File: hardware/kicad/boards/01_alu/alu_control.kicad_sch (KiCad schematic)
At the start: 8 parts, among them U155 KM28C64A, U156 KM28C64A, U171 74AHC541, U172 74AHC541

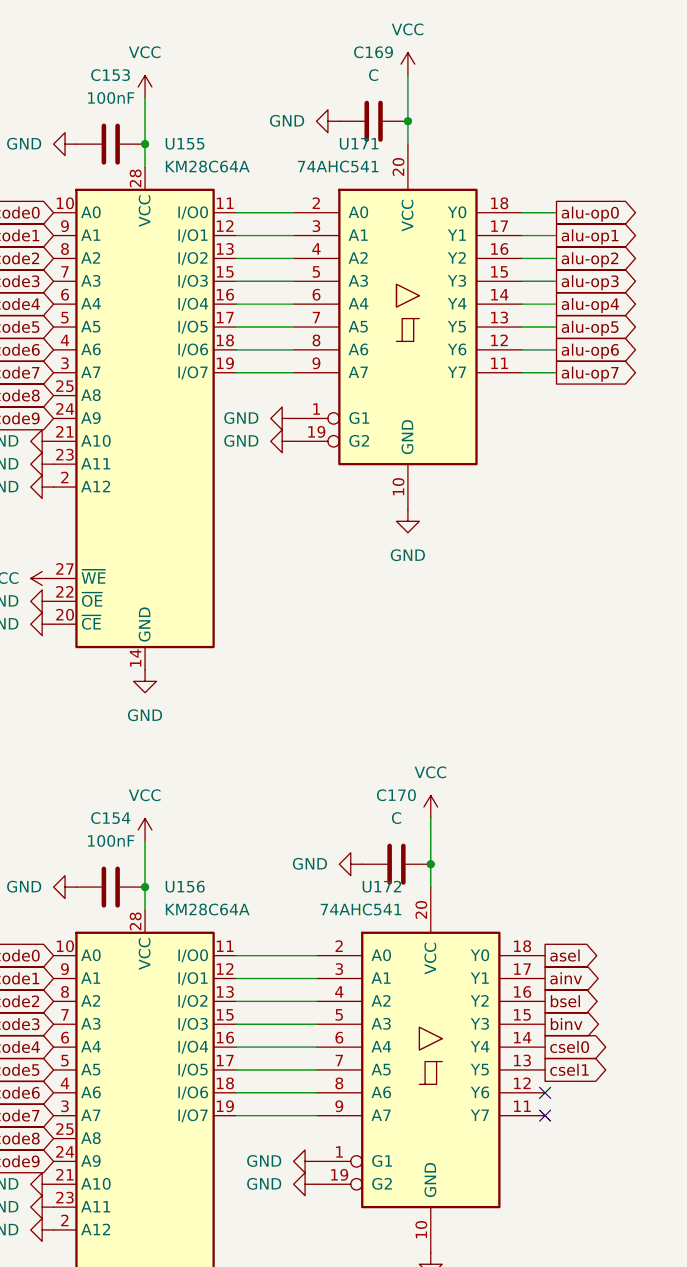
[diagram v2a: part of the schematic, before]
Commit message: refactor: improved global labeling and reduced ERC from 300+ to 6 power flags and minor connector in errors
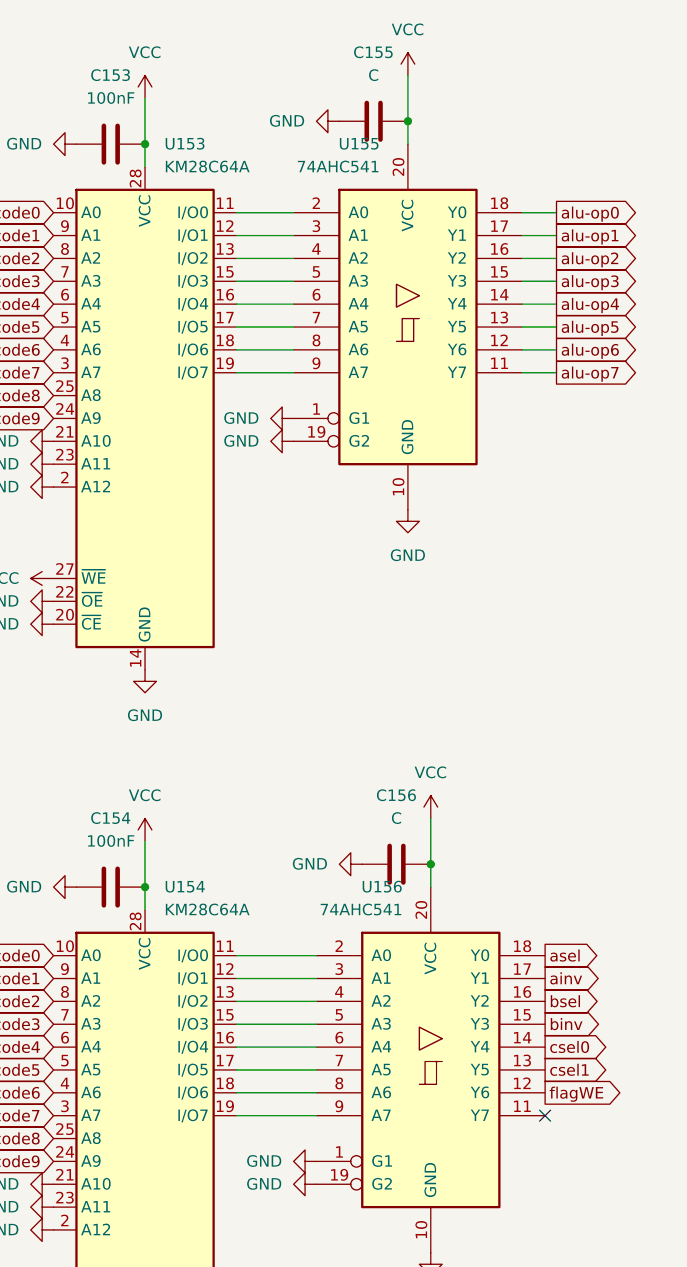
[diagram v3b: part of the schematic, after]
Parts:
- renumbered C169 to C155, C170 to C156, U155 to U153, U156 to U154, U171 to U155, U172 to U156
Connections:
- net flagWE: now reaches U156.12 (Y6)
- no-connect marks 2 -> 1
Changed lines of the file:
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@@
 		(at 95.25 153.67)
 	)
-	(no_connect
-		(at 95.25 151.13)
-	)
 	(wire
 		(pts
@@
 		)
 	)
+	(global_label "flagWE"
+		(shape output)
+		(at 95.25 151.13 0)
+		(fields_autoplaced yes)
+		(effects
+			(font
+				(size 1.27 1.27)
+			)
+			(justify left)
+		)
+		(property "Intersheetrefs" "${INTERSHEET_REFS}"
+			(at 104.5245 151.13 0)
+			(hide yes)
+			(show_name no)
+			(do_not_autoplace no)
+			(effects
+				(font
+					(size 1.27 1.27)
+				)
+				(justify left)
+			)
+		)
+	)
 	(global_label "ir-opcode2"
 		(shape input)
@@
 		(dnp no)
 		(fields_autoplaced yes)
-		(property "Reference" "#PWR0606"
+		(property "Reference" "#PWR0613"
 			(at 50.8 44.45 0)
 			(hide yes)
@@
 			(project "alu-32b"
 				(path "/ddad1417-0afc-402d-a021-92fc87ddd78a/debb55b2-e83b-4da4-bee0-8e5db8b77a4f"
-					(reference "#PWR0606")
+					(reference "#PWR0613")
 					(unit 1)
 				)
@@
 		(dnp no)
 		(fields_autoplaced yes)
-		(property "Reference" "#PWR0613"
+		(property "Reference" "#PWR0610"
 			(at 34.29 181.61 0)
 			(hide yes)
@@
 			(project "alu-32b"
 				(path "/ddad1417-0afc-402d-a021-92fc87ddd78a/debb55b2-e83b-4da4-bee0-8e5db8b77a4f"
-					(reference "#PWR0613")
+					(reference "#PWR0610")
 					(unit 1)
 				)
@@
 		(dnp no)
 		(fields_autoplaced yes)
-		(property "Reference" "#PWR0673"
+		(property "Reference" "#PWR0620"
 			(at 63.5 161.29 0)
 			(hide yes)
@@
 			(project "alu-32b"
 				(path "/ddad1417-0afc-402d-a021-92fc87ddd78a/debb55b2-e83b-4da4-bee0-8e5db8b77a4f"
-					(reference "#PWR0673")
+					(reference "#PWR0620")
 					(unit 1)
 				)
@@
 		(dnp no)
 		(fields_autoplaced yes)
-		(property "Reference" "#PWR0675"
+		(property "Reference" "#PWR0625"
 			(at 82.55 124.46 0)
 			(hide yes)
@@
 			(project "alu-32b"
 				(path "/ddad1417-0afc-402d-a021-92fc87ddd78a/debb55b2-e83b-4da4-bee0-8e5db8b77a4f"
-					(reference "#PWR0675")
+					(reference "#PWR0625")
 					(unit 1)
 				)
@@
 		(dnp no)
 		(fields_autoplaced yes)
-		(property "Reference" "U155"
+		(property "Reference" "U153"
 			(at 52.9433 45.72 0)
 			(show_name no)
@@
 			(project "alu-32b"
 				(path "/ddad1417-0afc-402d-a021-92fc87ddd78a/debb55b2-e83b-4da4-bee0-8e5db8b77a4f"
-					(reference "U155")
+					(reference "U153")
 					(unit 1)
 				)
@@
 		(dnp no)
 		(fields_autoplaced yes)
-		(property "Reference" "#PWR0669"
+		(property "Reference" "#PWR0618"
 			(at 60.96 78.74 0)
 			(hide yes)
@@
 			(project "alu-32b"
 				(path "/ddad1417-0afc-402d-a021-92fc87ddd78a/debb55b2-e83b-4da4-bee0-8e5db8b77a4f"
-					(reference "#PWR0669")
+					(reference "#PWR0618")
 					(unit 1)
 				)
@@
 		(dnp no)
 		(fields_autoplaced yes)
-		(property "Reference" "#PWR0610"
+		(property "Reference" "#PWR0607"
 			(at 34.29 166.37 0)
 			(hide yes)
@@
 			(project "alu-32b"
 				(path "/ddad1417-0afc-402d-a021-92fc87ddd78a/debb55b2-e83b-4da4-bee0-8e5db8b77a4f"
-					(reference "#PWR0610")
+					(reference "#PWR0607")
 					(unit 1)
 				)
@@
 		(dnp no)
 		(fields_autoplaced yes)
-		(property "Reference" "#PWR0609"
+		(property "Reference" "#PWR0606"
 			(at 34.29 163.83 0)
 			(hide yes)
@@
 			(project "alu-32b"
 				(path "/ddad1417-0afc-402d-a021-92fc87ddd78a/debb55b2-e83b-4da4-bee0-8e5db8b77a4f"
-					(reference "#PWR0609")
+					(reference "#PWR0606")
 					(unit 1)
 				)
@@
 		(dnp no)
 		(fields_autoplaced yes)
-		(property "Reference" "#PWR0670"
+		(property "Reference" "#PWR0621"
 			(at 66.04 43.18 0)
 			(hide yes)
@@
 			(project "alu-32b"
 				(path "/ddad1417-0afc-402d-a021-92fc87ddd78a/debb55b2-e83b-4da4-bee0-8e5db8b77a4f"
-					(reference "#PWR0670")
+					(reference "#PWR0621")
 					(unit 1)
 				)
@@
 		(in_pos_files yes)
 		(dnp no)
-		(property "Reference" "U172"
+		(property "Reference" "U156"
 			(at 79.4319 128.27 0)
 			(show_name no)
@@
 			(project "alu-32b"
 				(path "/ddad1417-0afc-402d-a021-92fc87ddd78a/debb55b2-e83b-4da4-bee0-8e5db8b77a4f"
-					(reference "U172")
+					(reference "U156")
 					(unit 1)
 				)
@@
 		(in_pos_files yes)
 		(dnp no)
-		(property "Reference" "U171"
+		(property "Reference" "U155"
 			(at 76.8919 45.72 0)
 			(show_name no)
@@
 			(project "alu-32b"
 				(path "/ddad1417-0afc-402d-a021-92fc87ddd78a/debb55b2-e83b-4da4-bee0-8e5db8b77a4f"
-					(reference "U171")
+					(reference "U155")
 					(unit 1)
 				)
@@
 		(dnp no)
 		(fields_autoplaced yes)
-		(property "Reference" "#PWR0671"
+		(property "Reference" "#PWR0623"
 			(at 80.01 41.91 0)
 			(hide yes)
@@
 			(project "alu-32b"
 				(path "/ddad1417-0afc-402d-a021-92fc87ddd78a/debb55b2-e83b-4da4-bee0-8e5db8b77a4f"
-					(reference "#PWR0671")
+					(reference "#PWR0623")
 					(unit 1)
 				)
@@
 		(dnp no)
 		(fields_autoplaced yes)
-		(property "Reference" "U156"
+		(property "Reference" "U154"
 			(at 52.9433 128.27 0)
 			(show_name no)
@@
 			(project "alu-32b"
 				(path "/ddad1417-0afc-402d-a021-92fc87ddd78a/debb55b2-e83b-4da4-bee0-8e5db8b77a4f"
-					(reference "U156")
+					(reference "U154")
 					(unit 1)
 				)
@@
 		(dnp no)
 		(fields_autoplaced yes)
-		(property "Reference" "C169"
+		(property "Reference" "C155"
 			(at 76.2 35.56 90)
 			(show_name no)
@@
 			(project "alu-32b"
 				(path "/ddad1417-0afc-402d-a021-92fc87ddd78a/debb55b2-e83b-4da4-bee0-8e5db8b77a4f"
-					(reference "C169")
+					(reference "C155")
 					(unit 1)
 				)
@@
 		(dnp no)
 		(fields_autoplaced yes)
-		(property "Reference" "#PWR0608"
+		(property "Reference" "#PWR0605"
 			(at 34.29 161.29 0)
 			(hide yes)
@@
 			(project "alu-32b"
 				(path "/ddad1417-0afc-402d-a021-92fc87ddd78a/debb55b2-e83b-4da4-bee0-8e5db8b77a4f"
-					(reference "#PWR0608")
+					(reference "#PWR0605")
 					(unit 1)
 				)
@@
 		(dnp no)
 		(fields_autoplaced yes)
-		(property "Reference" "#PWR0614"
+		(property "Reference" "#PWR0612"
 			(at 36.83 128.27 0)
 			(hide yes)
@@
 			(project "alu-32b"
 				(path "/ddad1417-0afc-402d-a021-92fc87ddd78a/debb55b2-e83b-4da4-bee0-8e5db8b77a4f"
-					(reference "#PWR0614")
+					(reference "#PWR0612")
 					(unit 1)
 				)
@@
 		(dnp no)
 		(fields_autoplaced yes)
-		(property "Reference" "#PWR0667"
+		(property "Reference" "#PWR0624"
 			(at 80.01 92.71 0)
 			(hide yes)
@@
 			(project "alu-32b"
 				(path "/ddad1417-0afc-402d-a021-92fc87ddd78a/debb55b2-e83b-4da4-bee0-8e5db8b77a4f"
-					(reference "#PWR0667")
+					(reference "#PWR0624")
 					(unit 1)
 				)
@@
 		(dnp no)
 		(fields_autoplaced yes)
-		(property "Reference" "C170"
+		(property "Reference" "C156"
 			(at 78.74 118.11 90)
 			(show_name no)
@@
 			(project "alu-32b"
 				(path "/ddad1417-0afc-402d-a021-92fc87ddd78a/debb55b2-e83b-4da4-bee0-8e5db8b77a4f"
-					(reference "C170")
+					(reference "C156")
 					(unit 1)
 				)
@@
 		(dnp no)
 		(fields_autoplaced yes)
-		(property "Reference" "#PWR0676"
+		(property "Reference" "#PWR0626"
 			(at 82.55 175.26 0)
 			(hide yes)
@@
 			(project "alu-32b"
 				(path "/ddad1417-0afc-402d-a021-92fc87ddd78a/debb55b2-e83b-4da4-bee0-8e5db8b77a4f"
-					(reference "#PWR0676")
+					(reference "#PWR0626")
 					(unit 1)
 				)
@@
 		(dnp no)
 		(fields_autoplaced yes)
-		(property "Reference" "#PWR0674"
+		(property "Reference" "#PWR0622"
 			(at 68.58 125.73 0)
 			(hide yes)
@@
 			(project "alu-32b"
 				(path "/ddad1417-0afc-402d-a021-92fc87ddd78a/debb55b2-e83b-4da4-bee0-8e5db8b77a4f"
-					(reference "#PWR0674")
+					(reference "#PWR0622")
 					(unit 1)
 				)
@@
 		(dnp no)
 		(fields_autoplaced yes)
-		(property "Reference" "#PWR0672"
+		(property "Reference" "#PWR0619"
 			(at 63.5 158.75 0)
 			(hide yes)
@@
 			(project "alu-32b"
 				(path "/ddad1417-0afc-402d-a021-92fc87ddd78a/debb55b2-e83b-4da4-bee0-8e5db8b77a4f"
-					(reference "#PWR0672")
+					(reference "#PWR0619")
 					(unit 1)
 				)
@@
 		(dnp no)
 		(fields_autoplaced yes)
-		(property "Reference" "#PWR0605"
+		(property "Reference" "#PWR0611"
 			(at 36.83 45.72 0)
 			(hide yes)
@@
 			(project "alu-32b"
 				(path "/ddad1417-0afc-402d-a021-92fc87ddd78a/debb55b2-e83b-4da4-bee0-8e5db8b77a4f"
-					(reference "#PWR0605")
+					(reference "#PWR0611")
 					(unit 1)
 				)
@@
 		(dnp no)
 		(fields_autoplaced yes)
-		(property "Reference" "#PWR0607"
+		(property "Reference" "#PWR0614"
 			(at 50.8 110.49 0)
 			(hide yes)
@@
 			(project "alu-32b"
 				(path "/ddad1417-0afc-402d-a021-92fc87ddd78a/debb55b2-e83b-4da4-bee0-8e5db8b77a4f"
-					(reference "#PWR0607")
+					(reference "#PWR0614")
 					(unit 1)
 				)
@@
 		(dnp no)
 		(fields_autoplaced yes)
-		(property "Reference" "#PWR0612"
+		(property "Reference" "#PWR0609"
 			(at 34.29 179.07 0)
 			(hide yes)
@@
 			(project "alu-32b"
 				(path "/ddad1417-0afc-402d-a021-92fc87ddd78a/debb55b2-e83b-4da4-bee0-8e5db8b77a4f"
-					(reference "#PWR0612")
+					(reference "#PWR0609")
 					(unit 1)
 				)
@@
 		(dnp no)
 		(fields_autoplaced yes)
-		(property "Reference" "#PWR0611"
+		(property "Reference" "#PWR0608"
 			(at 44.45 176.53 0)
 			(hide yes)
@@
 			(project "alu-32b"
 				(path "/ddad1417-0afc-402d-a021-92fc87ddd78a/debb55b2-e83b-4da4-bee0-8e5db8b77a4f"
-					(reference "#PWR0611")
+					(reference "#PWR0608")
 					(unit 1)
 				)
@@
 		(dnp no)
 		(fields_autoplaced yes)
-		(property "Reference" "#PWR0668"
+		(property "Reference" "#PWR0617"
 			(at 60.96 76.2 0)
 			(hide yes)
@@
 			(project "alu-32b"
 				(path "/ddad1417-0afc-402d-a021-92fc87ddd78a/debb55b2-e83b-4da4-bee0-8e5db8b77a4f"
-					(reference "#PWR0668")
+					(reference "#PWR0617")
 					(unit 1)
 				)
